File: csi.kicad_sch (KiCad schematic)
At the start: 5 parts, among them J1 Conn_FFC_WE_68715014022_CUSTO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

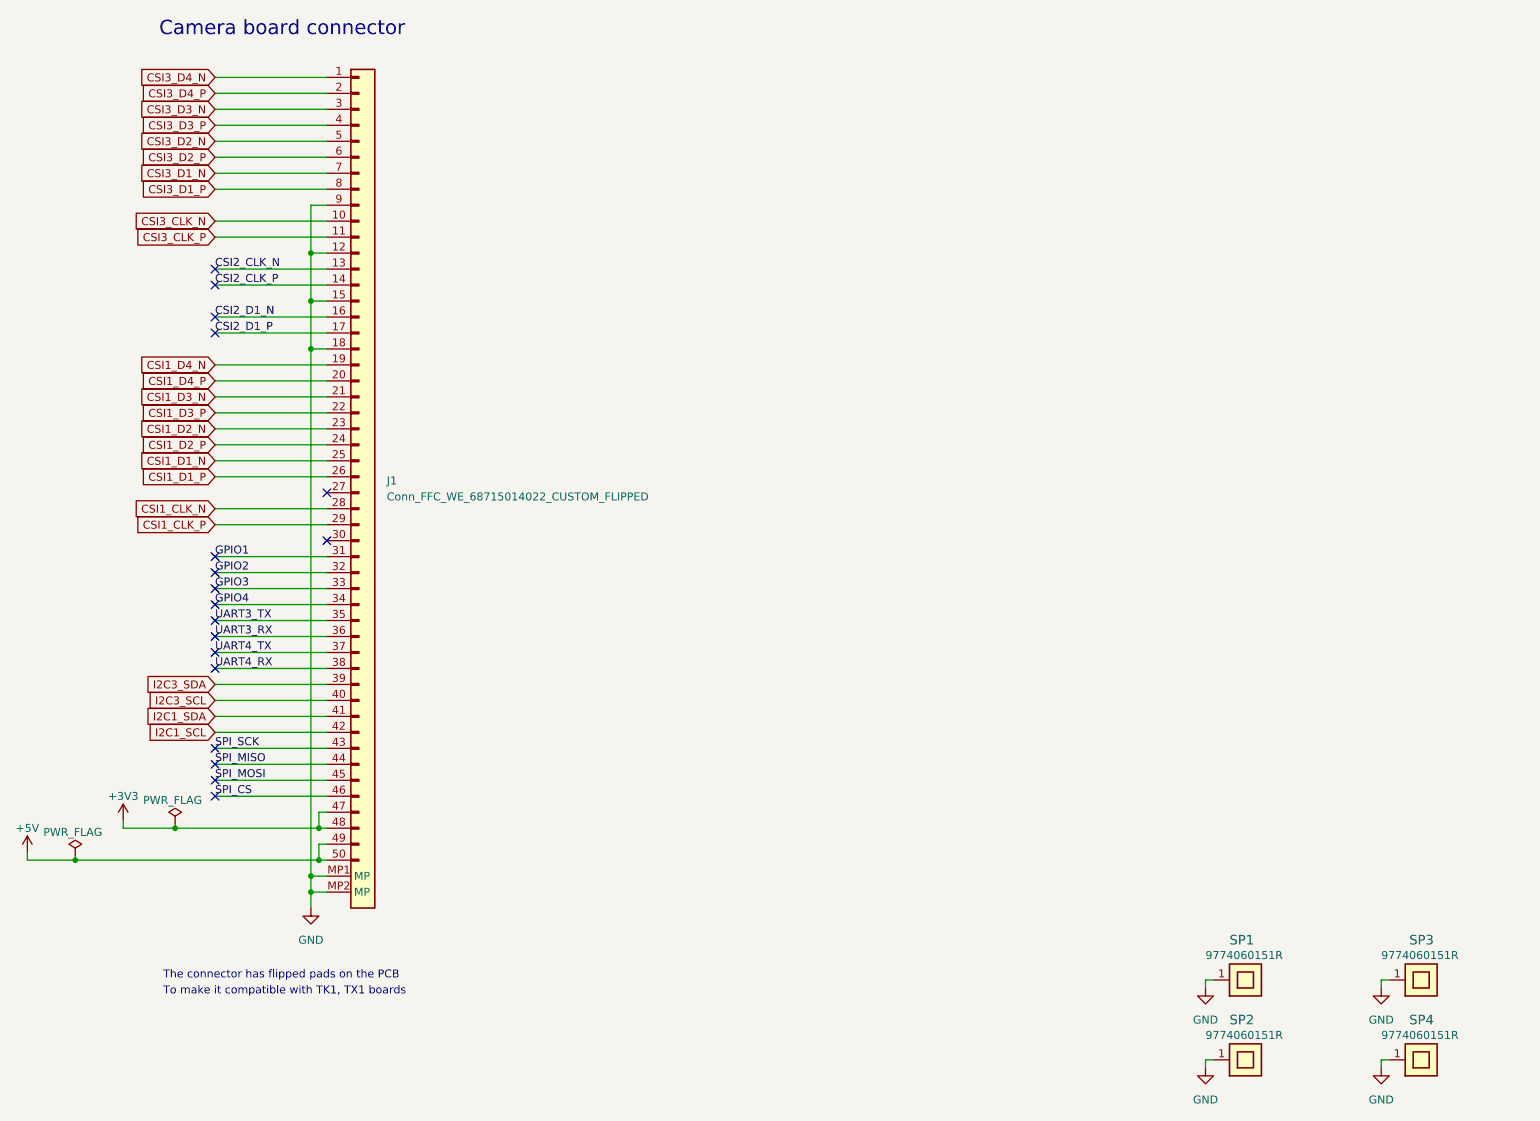
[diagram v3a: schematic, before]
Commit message: [#58304] Revert flipping J6
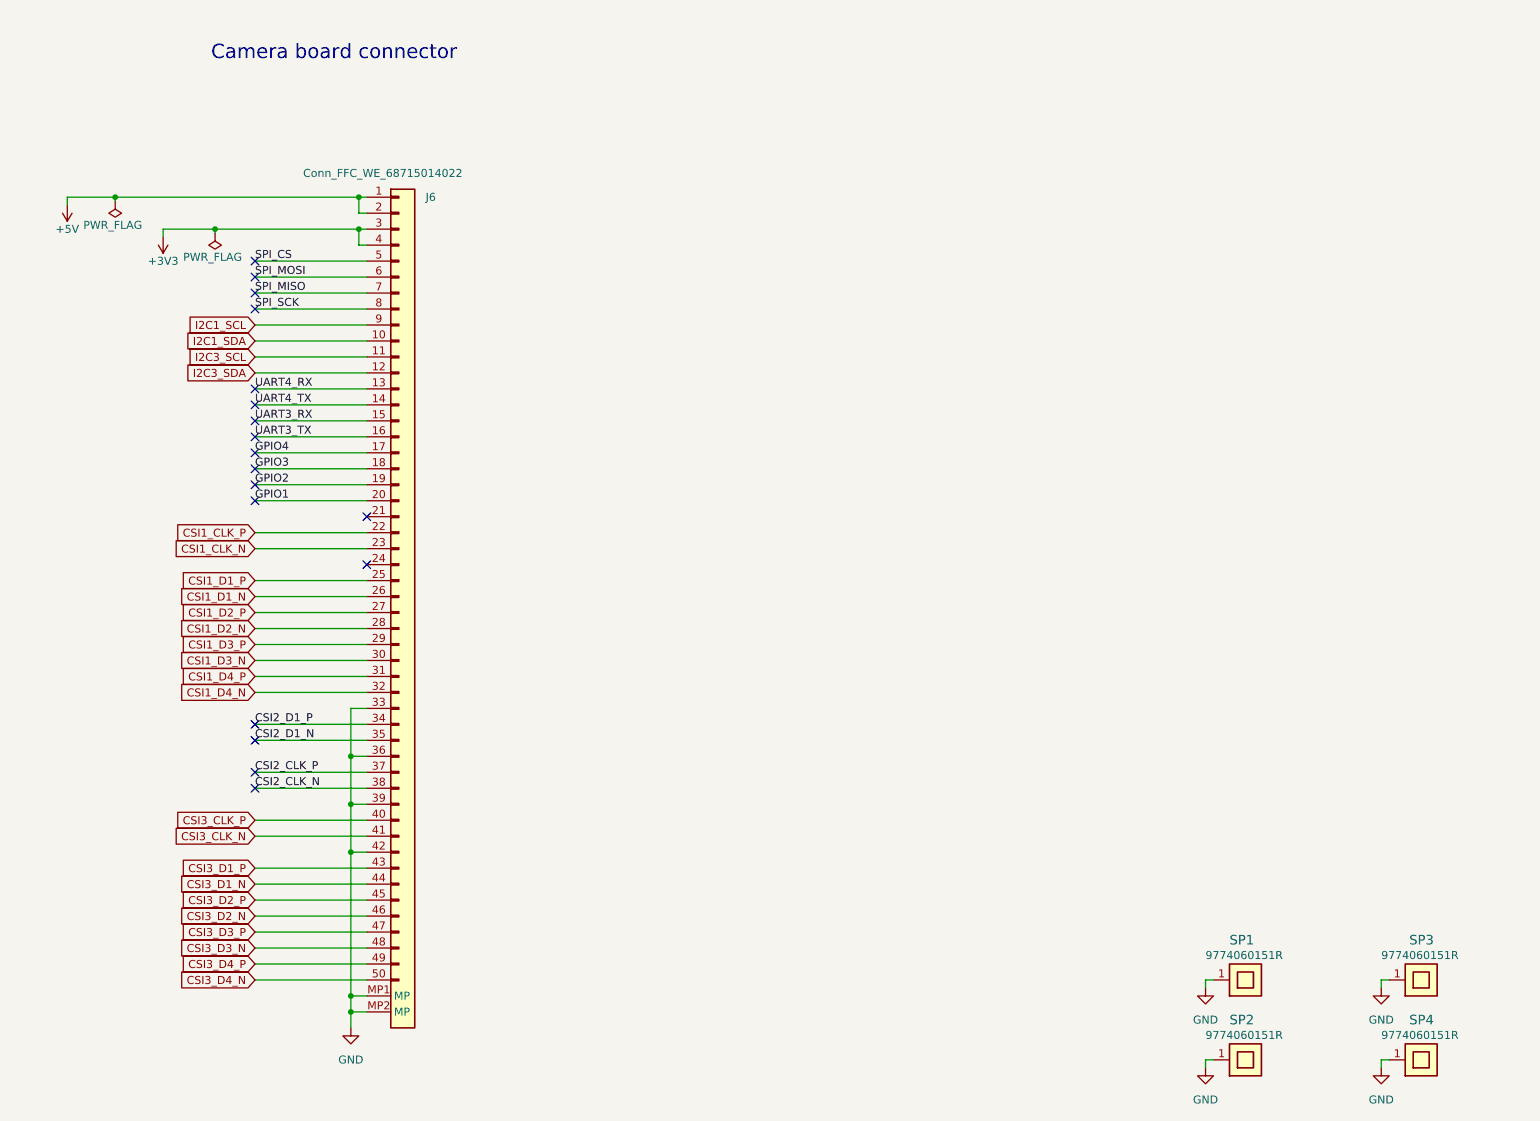
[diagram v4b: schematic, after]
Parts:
- removed J1: Conn_FFC_WE_68715014022_CUSTOM_FLIPPED, antmicro-footprints:Conn_FFC_WE_68715014x22_CUSTOM_FLIPPED, symbol antmicroFCCConnectors:Conn_FFC_WE_68715014022_CUSTOM_FLIPPED
- added J6: Conn_FFC_WE_68715014022, antmicro-footprints:Conn_FFC_WE_68715014x22, symbol antmicroFCCConnectors:Conn_FFC_WE_68715014022
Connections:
- net +3V3: now also J6.3, J6.4
- net +5V: now also J6.1, J6.2
- net CSI1_CLK_N: now also J6.23
- net CSI1_CLK_P: now also J6.22
- net CSI1_D1_N: now also J6.26
- net CSI1_D1_P: now also J6.25
- net CSI1_D2_N: now also J6.28
- net CSI1_D2_P: now also J6.27
- net CSI1_D3_N: now also J6.30
- net CSI1_D3_P: now also J6.29
- net CSI1_D4_N: now also J6.32
- net CSI1_D4_P: now also J6.31
- net CSI2_CLK_N: now also J6.38
- net CSI2_CLK_P: now also J6.37
- net CSI2_D1_N: now also J6.35
- net CSI2_D1_P: now also J6.34
- net CSI3_CLK_N: now also J6.41
- net CSI3_CLK_P: now also J6.40
- net CSI3_D1_N: now also J6.44
- net CSI3_D1_P: now also J6.43
- net CSI3_D2_N: now also J6.46
- net CSI3_D2_P: now also J6.45
- net CSI3_D3_N: now also J6.48
- net CSI3_D3_P: now also J6.47
- net CSI3_D4_N: now also J6.50
- net CSI3_D4_P: now also J6.49
- net GND: now also J6.33, J6.36, J6.39, J6.42, J6.MP1 (MP), J6.MP2 (MP)
- net GPIO1: now also J6.20
- net GPIO2: now also J6.19
- net GPIO3: now also J6.18
- net GPIO4: now also J6.17
- net I2C1_SCL: now also J6.9
- net I2C1_SDA: now also J6.10
- net I2C3_SCL: now also J6.11
- net I2C3_SDA: now also J6.12
- net SPI_CS: now also J6.5
- net SPI_MISO: now also J6.7
- net SPI_MOSI: now also J6.6
- net SPI_SCK: now also J6.8
- net UART3_RX: now also J6.15
- net UART3_TX: now also J6.16
- net UART4_RX: now also J6.13
- net UART4_TX: now also J6.14
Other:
- note removed: "The connector has flipped pads on the PCB"
- note removed: "To make it compatible with TK1, TX1 boards"
